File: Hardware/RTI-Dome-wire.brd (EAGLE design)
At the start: 80 x 71.1 mm, 34 parts, among them IC2 74LVC244

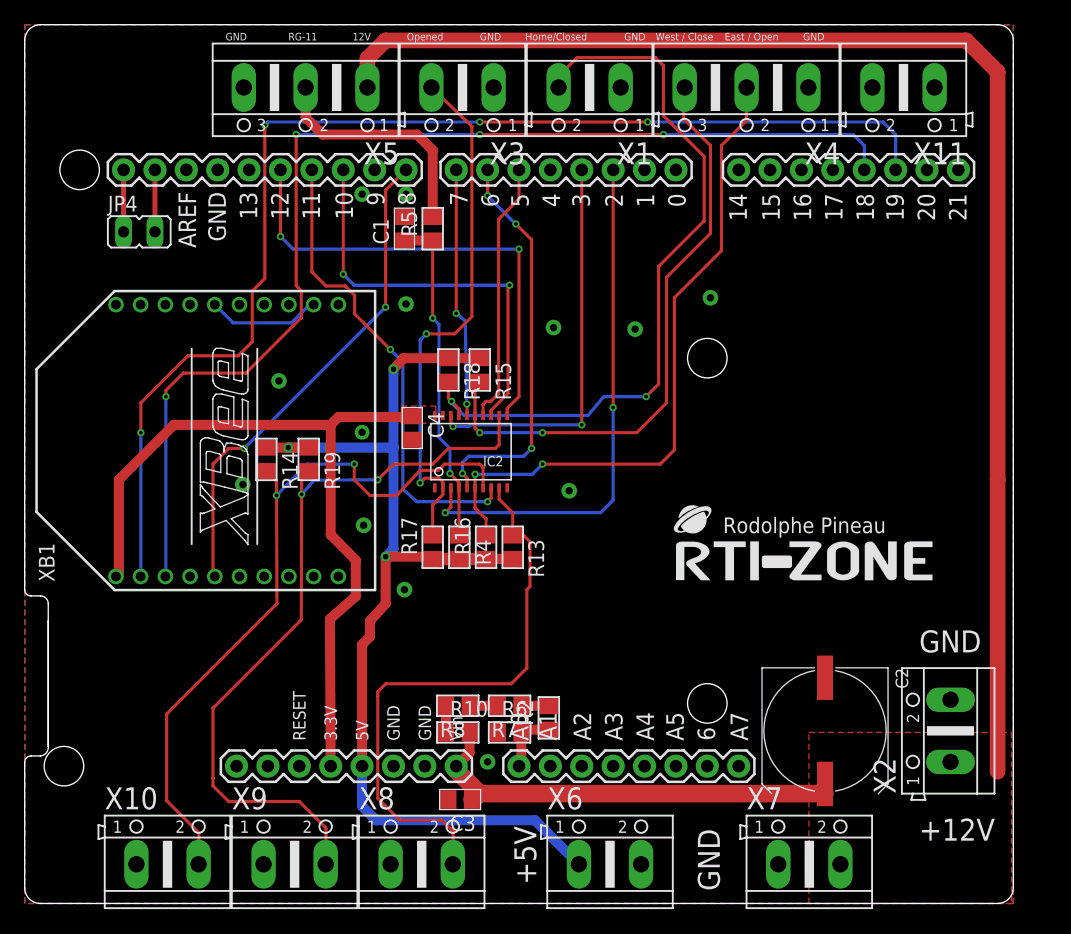
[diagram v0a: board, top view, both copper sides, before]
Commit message: Auto detect shutter presence.
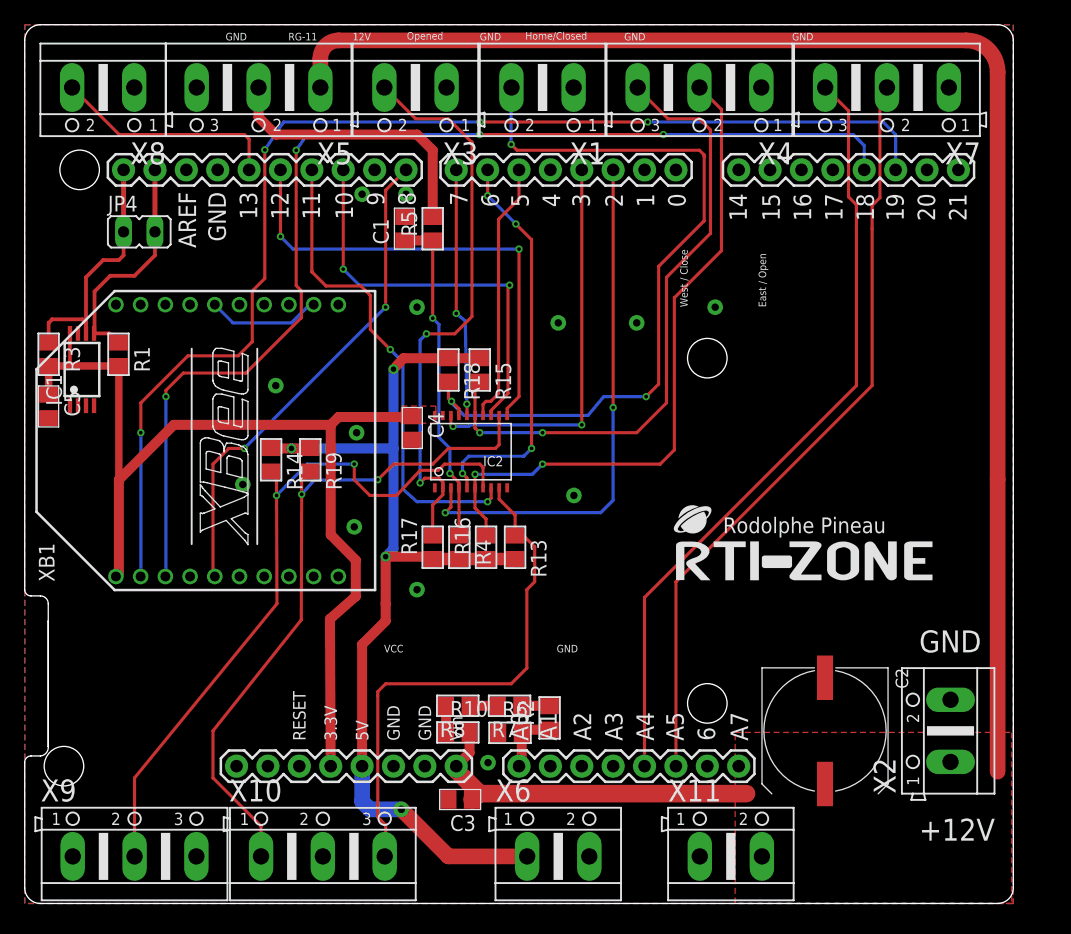
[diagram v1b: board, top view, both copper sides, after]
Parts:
- added C5: 100nF, rti:C0805
- added IC1: 24AA128ST, microchip:TSSOP8
- added R1, R3: 1K, rti:R0805
- X10, X7, X9: device con-ptr500:AK500/2 -> con-ptr500:AK500/3
- moved X8 67.9 mm to (6.35, 66.0), turned to 180 degrees
- moved X11 63.8 mm to (57.1, 3.81), turned to 0 degrees
- moved X7 63.2 mm to (69.8, 66.0), turned to 180 degrees
- moved X9 13.0 mm to (8.89, 3.81)
- moved X10 12.6 mm to (24.1, 3.81)
- moved X6 4.24 mm to (43.2, 3.81)
- moved X1 3.81 mm to (41.9, 66.0)
- moved X4 3.81 mm to (54.6, 66.0)
- moved X5 3.81 mm to (18.9, 66.0)
- moved X3 3.81 mm to (31.6, 66.0)
- moved R14 0.38 mm to (19.9, 35.9)
- moved R13 0.19 mm to (39.7, 28.8)
- moved R19 0.13 mm to (23.1, 35.9)
- moved R2 0.06 mm to (42.5, 15.0)
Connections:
- removed net 13: PCB1.13
- removed net N$6: JP4.1, PCB1.SCL1
- removed net N$8: JP4.2, PCB1.SDA1
- new net D13: PCB1.13, X8.2
- new net SCL: IC1.6, JP4.1, PCB1.SCL1, R3.1
- new net SDA: IC1.5, JP4.2, PCB1.SDA1, R1.1
- net +12V: now also X11.2; no longer X7.2
- net 3.3V: now also C5.1, IC1.8, R1.2, R3.2
- net AT_PARK_PIN: now also X7.2; no longer X11.1
- net AT_PARK_PIN_LOOP: now also X7.3; no longer X11.2
- net GND: now also C5.2, IC1.1, IC1.2, IC1.3, IC1.4, X10.2, X11.1, X9.3; no longer X10.1
- net M_DIR_5V: now also X10.1; no longer X9.2
- net M_EN_5V: now also X9.2; no longer X10.2
- net M_STEP_5V: now also X10.3; no longer X8.2
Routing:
- net AT_PARK_PIN_LOOP: track 0.00 -> 63.1 mm
- net AT_PARK_PIN: track 0.00 -> 62.0 mm
- net SCL: track 0.00 -> 20.1 mm
- net 3.3V: track 63.3 -> 83.2 mm
- net SDA: track 0.00 -> 18.7 mm
- net D13: track 0.00 -> 18.5 mm
- net M_DIR_5V: track 62.2 -> 55.6 mm
- net N$8: track 5.02 -> 0.00 mm
- net N$6: track 5.02 -> 0.00 mm
- net VCC: track 85.6 -> 80.6 mm, vias 3 -> 4
- net M_STEP_5V: track 47.6 -> 42.9 mm
- net RG-11-IN_EXT: track 19.2 -> 23.0 mm
- net BUTTON_WEST_CLOSE_5V: track 48.4 -> 51.5 mm
- net SHUTTER_OPENED_5V: track 43.3 -> 46.4 mm
- net +12V: track 146.6 -> 144.0 mm
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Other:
- board text added: "VCC"
- board text removed: "+5V"
- board text removed: "DIR+"
- board text removed: "EN+"
- board text removed: "STP+"

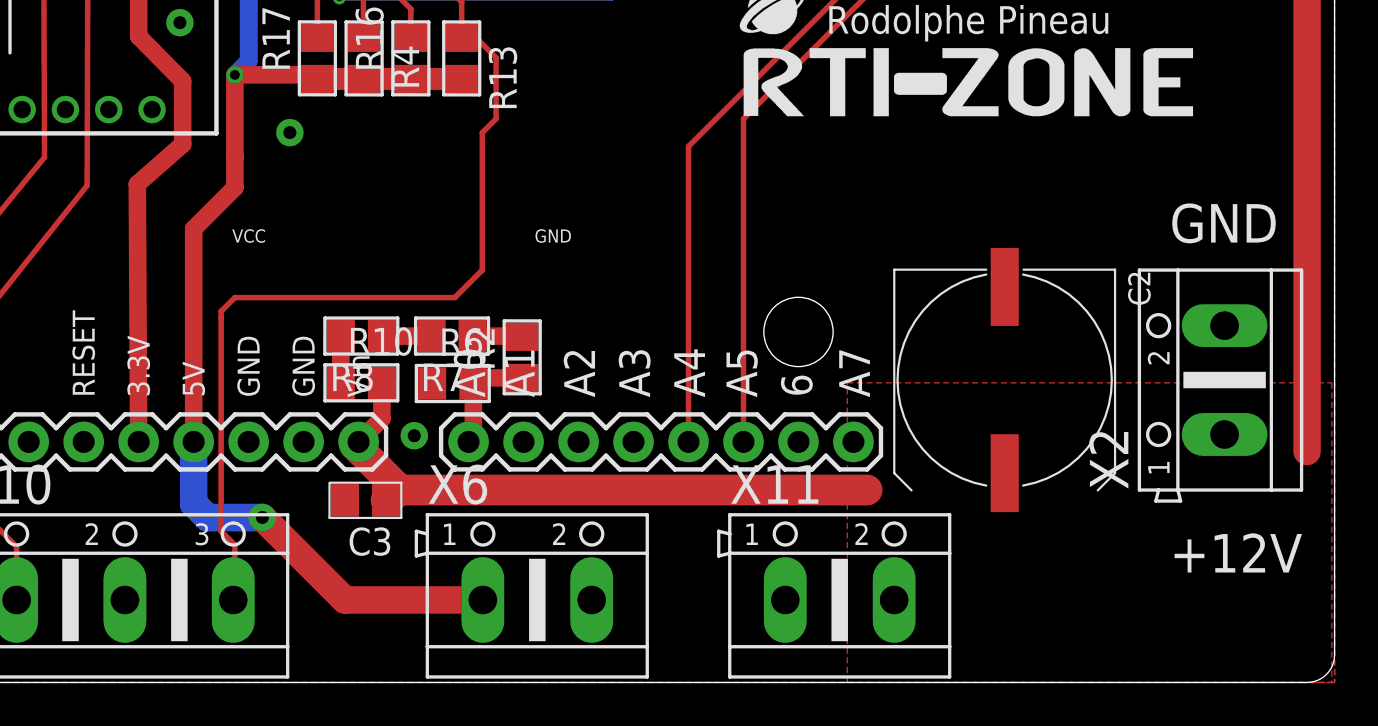
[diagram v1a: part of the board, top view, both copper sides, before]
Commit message: Tested the ISD04 stepper controller.. needed to add 3.3V header as the pull-up on the buffer output don't bring the signal to 5V and therefore the optocoupler in the contoller doesn't do the right thing.
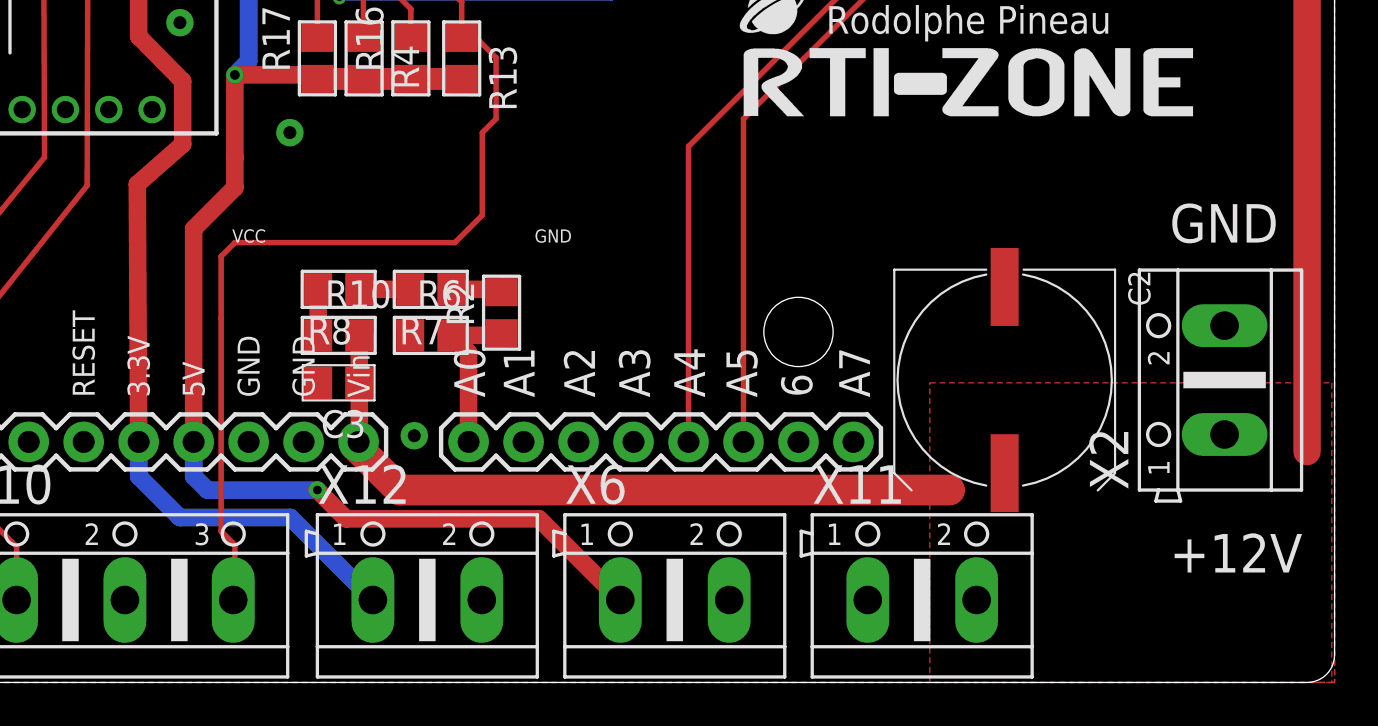
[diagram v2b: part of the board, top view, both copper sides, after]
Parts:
- added X12: (no value), con-ptr500:AK500/2
- moved X6 6.35 mm to (49.5, 3.81)
- moved C3 5.57 mm to (34.0, 13.8)
- moved X11 3.81 mm to (61.0, 3.81)
- moved R6 2.44 mm to (38.3, 16.0)
- moved R10 2.43 mm to (34.0, 16.0)
- moved R8 2.40 mm to (34.0, 18.2)
- moved R7 2.37 mm to (38.3, 18.2)
- moved R2 2.27 mm to (41.5, 17.1)
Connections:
- net 3.3V: now also X12.1
- net GND: now also X12.2
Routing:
- net 3.3V: track 83.2 -> 98.0 mm
- net VCC: track 80.6 -> 86.2 mm
- net +12V: track 144.0 -> 148.8 mm
- net VPIN: track 5.15 -> 7.61 mm

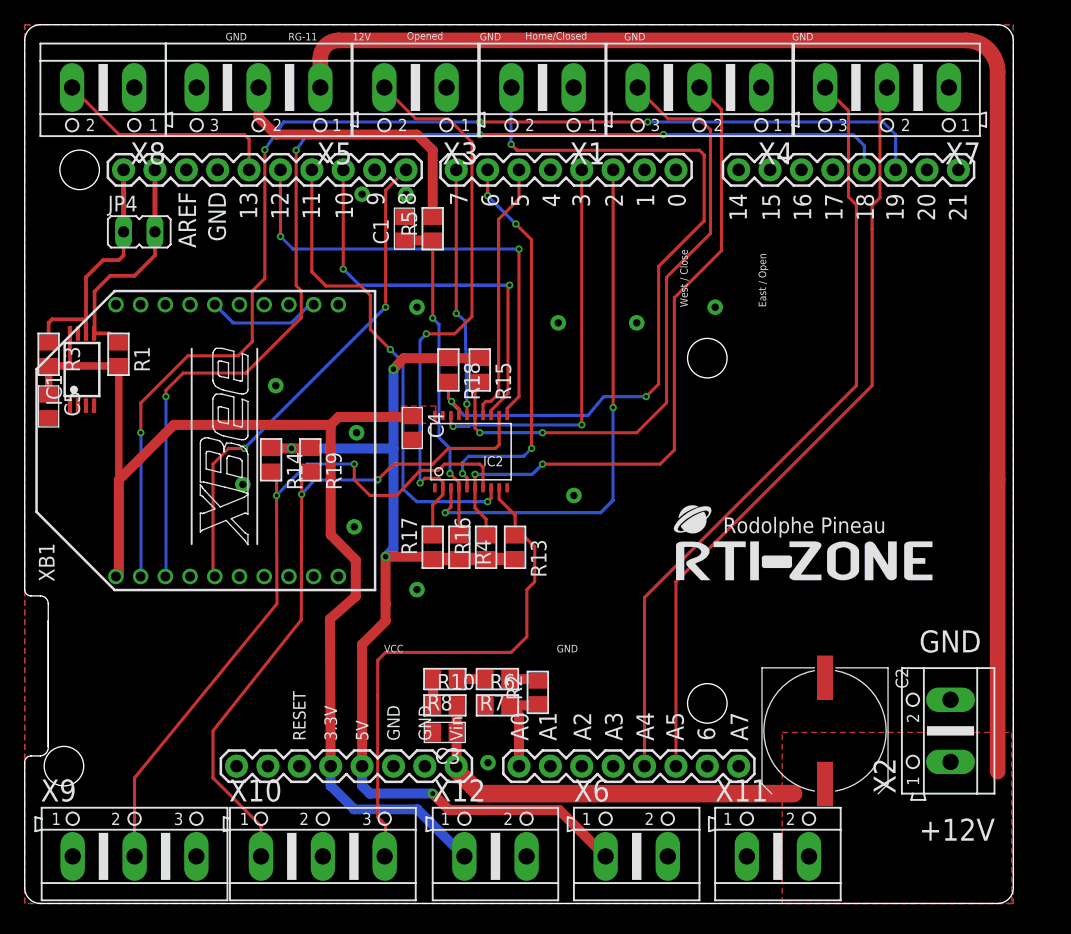
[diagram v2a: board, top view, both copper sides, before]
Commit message: Adding a usb-serial + usb port on SERIAL2 (pin 16 and 17)
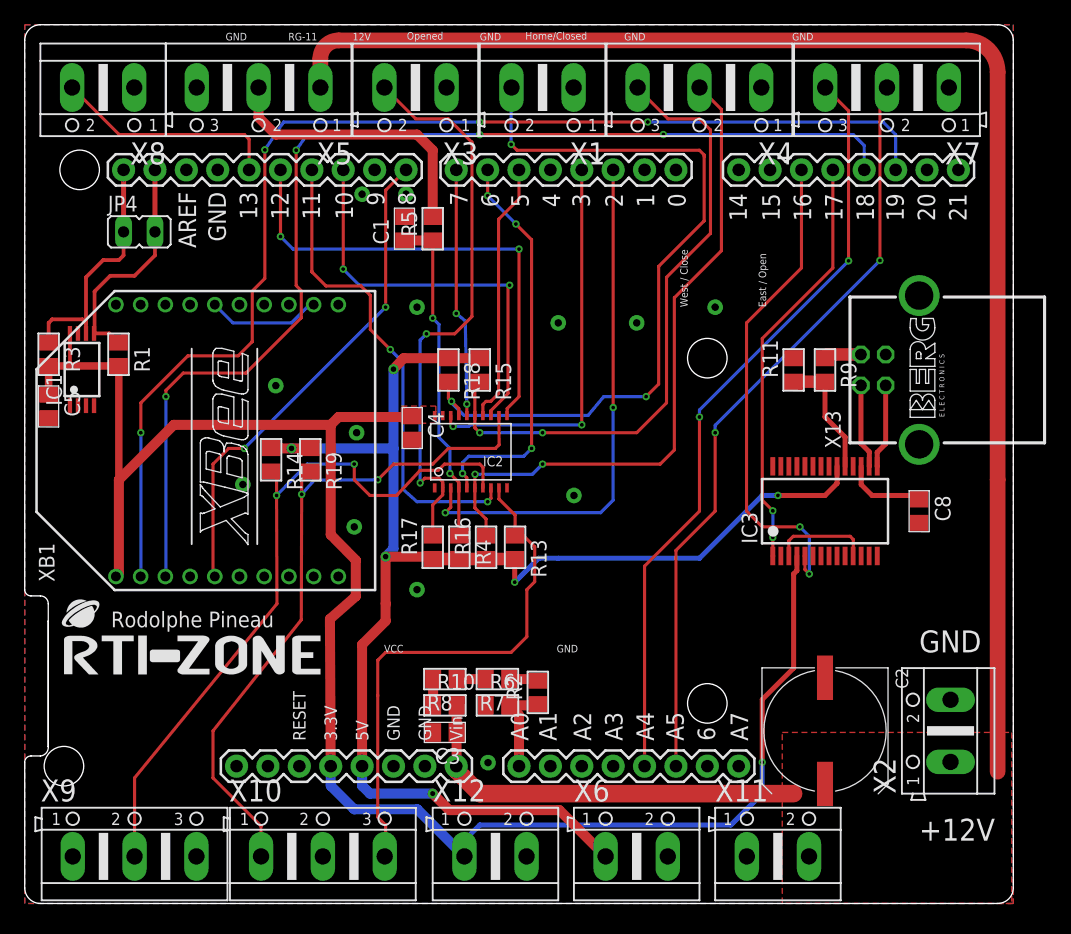
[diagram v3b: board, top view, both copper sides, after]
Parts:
- added C8: 100nF, rti:C0805
- added IC3: FT232RL, ftdichip:SSOP28
- added R11: 10K, rti:R0805
- added R9: 4.7K, rti:R0805
- added X13: PN61729-S, con-berg:PN61729-S
- moved U$4 50.1 mm to (3.17, 18.5)
- moved IC2 0.80 mm to (36.1, 36.6)
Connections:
- new net N$1: IC3.19, R11.1, R9.2
- new net N$21: IC3.10
- new net N$4: IC3.11, IC3.3
- new net N$6: C8.1, IC3.17
- new net RX2: IC3.1, PCB1.17
- new net TX2: IC3.5, PCB1.16
- new net USBDM: IC3.16, X13.2
- new net USBDP: IC3.15, X13.3
- new net USB_VCC: R9.1, X13.1
- net 3.3V: now also IC3.4
- net GND: now also C8.2, IC3.18, IC3.21, IC3.25, IC3.7, R11.2, X13.4, X13.S1, X13.S2
- net VCC: now also IC3.20
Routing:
- net 3.3V: track 98.0 -> 145.3 mm, vias 0 -> 1
- net TX2: track 0.00 -> 40.0 mm, vias 0 -> 2
- net RX2: track 0.00 -> 34.0 mm, vias 0 -> 2
- net VCC: track 86.2 -> 118.9 mm, vias 4 -> 6
- net N$1: track 0.00 -> 10.1 mm
- net N$4: track 0.00 -> 8.05 mm
- net USBDM: track 0.00 -> 6.84 mm
- net USBDP: track 0.00 -> 6.84 mm
- net N$6: track 0.00 -> 6.75 mm
- net USB_VCC: track 0.00 -> 3.08 mm
- net AT_PARK_PIN_LOOP: track 63.1 -> 62.5 mm, vias 0 -> 2
- net AT_PARK_PIN: vias 0 -> 2

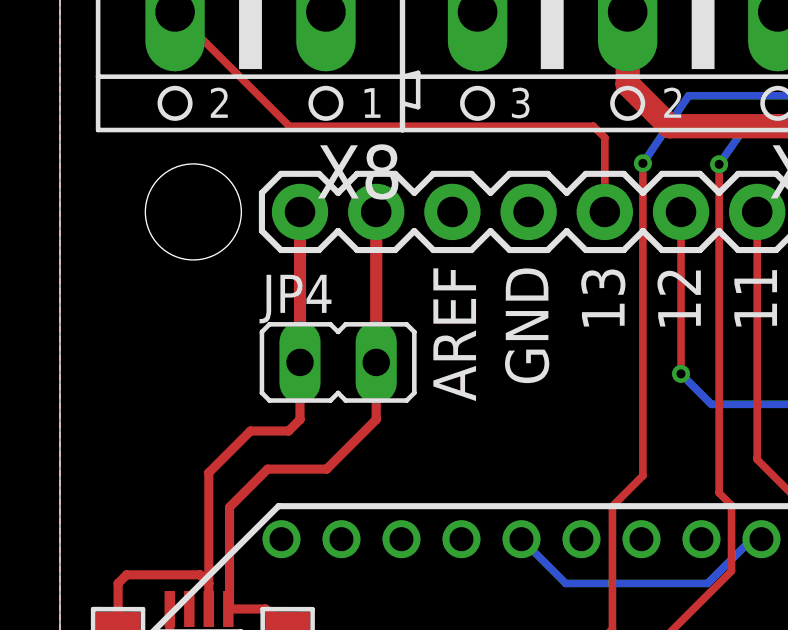
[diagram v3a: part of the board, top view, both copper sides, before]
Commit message: Remove I2C 2 pin header as we now have the eeprom on the board.
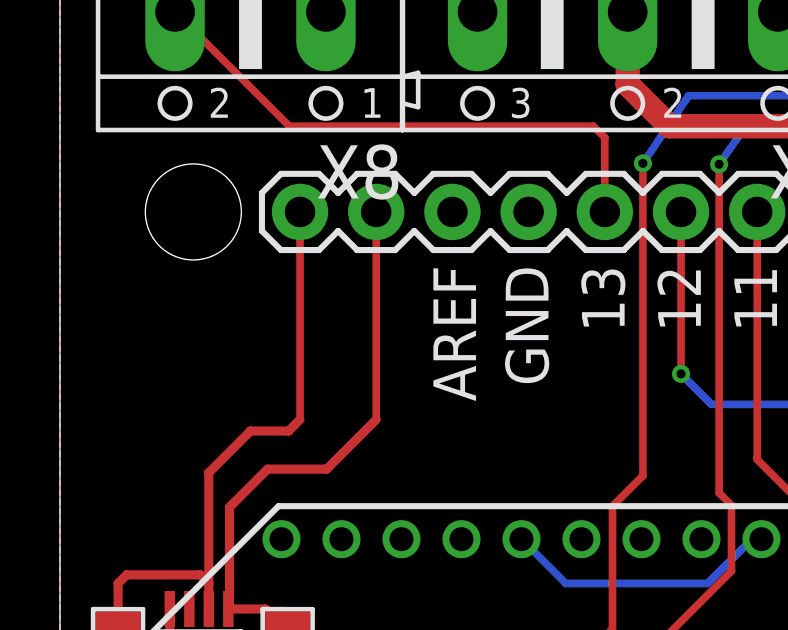
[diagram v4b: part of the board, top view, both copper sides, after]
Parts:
- removed JP4: (no value), jumper:JP1
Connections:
- net SCL: no longer JP4.1
- net SDA: no longer JP4.2
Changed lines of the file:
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@@
 <element name="C1" library="rti" package="C0805" value="10uF" x="30.734" y="54.61" rot="R90"/>
 <element name="R5" library="rti" package="R0805" value="100" x="33.02" y="54.61" rot="R90"/>
-<element name="JP4" library="jumper" package="JP1" value="" x="9.271" y="54.356" rot="R270"/>
 <element name="U$4" library="rti" package="LOGO_BIG" value="RTI-LOGO_BIG" x="3.175" y="18.542"/>
 <element name="C2" library="rti" package="UD-10X10_NICHICON" value="100uF" x="64.77" y="13.97" rot="R270"/>
@@
 <contactref element="IC1" pad="5"/>
 <contactref element="R1" pad="1"/>
-<contactref element="JP4" pad="2"/>
-<wire x1="10.541" y1="59.3725" x2="10.541" y2="54.356" width="0.4064" layer="1"/>
 <contactref element="PCB1" pad="SDA1"/>
-<wire x1="10.541" y1="54.356" x2="10.541" y2="52.451" width="0.3048" layer="1"/>
 <wire x1="10.541" y1="52.451" x2="8.89" y2="50.8" width="0.3048" layer="1"/>
 <wire x1="8.89" y1="50.8" x2="6.9215" y2="50.8" width="0.3048" layer="1"/>
@@
 <wire x1="7.58825" y1="45.4" x2="6.8515" y2="46.13675" width="0.3048" layer="1"/>
 <wire x1="6.8515" y1="46.13675" x2="5.6105" y2="46.13675" width="0.3048" layer="1"/>
+<wire x1="10.541" y1="59.3725" x2="10.541" y2="52.451" width="0.254" layer="1"/>
 </signal>
 <signal name="SCL">
 <contactref element="IC1" pad="6"/>
 <contactref element="R3" pad="1"/>
-<contactref element="JP4" pad="1"/>
-<wire x1="8.001" y1="59.3725" x2="8.001" y2="54.356" width="0.4064" layer="1"/>
 <contactref element="PCB1" pad="SCL1"/>
 <wire x1="4.9605" y1="46.13675" x2="4.9605" y2="46.99" width="0.3048" layer="1"/>
@@
 <wire x1="6.35" y1="52.07" x2="7.62" y2="52.07" width="0.3048" layer="1"/>
 <wire x1="7.62" y1="52.07" x2="8.001" y2="52.451" width="0.3048" layer="1"/>
-<wire x1="8.001" y1="52.451" x2="8.001" y2="54.356" width="0.3048" layer="1"/>
 <wire x1="1.93675" y1="45.4" x2="1.93675" y2="46.99" width="0.3048" layer="1"/>
 <wire x1="1.93675" y1="46.99" x2="2.2225" y2="47.27575" width="0.3048" layer="1"/>
 <wire x1="2.2225" y1="47.27575" x2="4.67475" y2="47.27575" width="0.3048" layer="1"/>
 <wire x1="4.67475" y1="47.27575" x2="4.9605" y2="46.99" width="0.3048" layer="1"/>
+<wire x1="8.001" y1="59.3725" x2="8.001" y2="52.451" width="0.254" layer="1"/>
 </signal>
 <signal name="D13">
